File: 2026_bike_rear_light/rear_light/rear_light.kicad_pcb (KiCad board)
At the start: 2 copper layers, 22 parts, among them J1 Conn_01x04, J2 Conn_01x05, Q1 2N5551, Q2 FQP27P06, Q3 2N5551, Q4 FQP27P06, Q5 2N5551, Q6 2N5551, Q7 FQP27P06, U1 YAAJ_DCDC_StepDown_LM2596

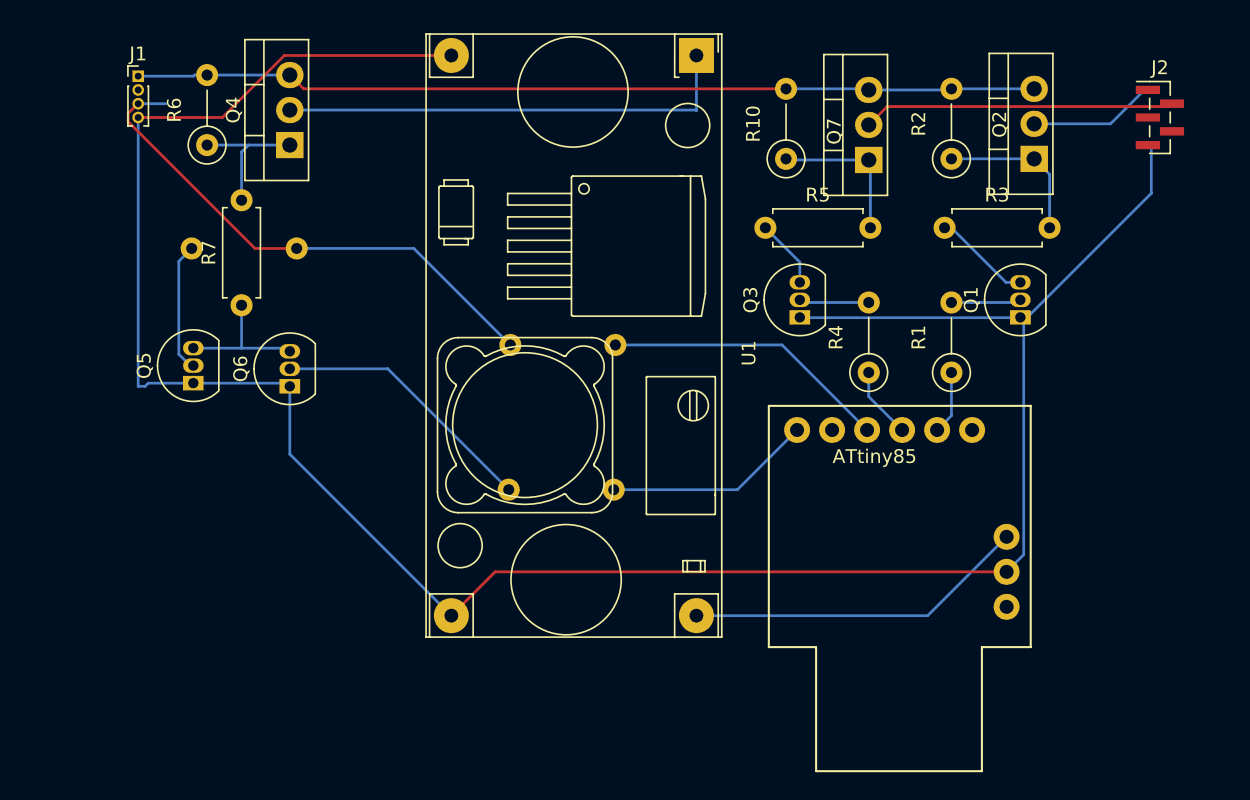
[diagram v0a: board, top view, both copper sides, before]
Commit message: Bike Rear Light - Update PCB for molex connectors
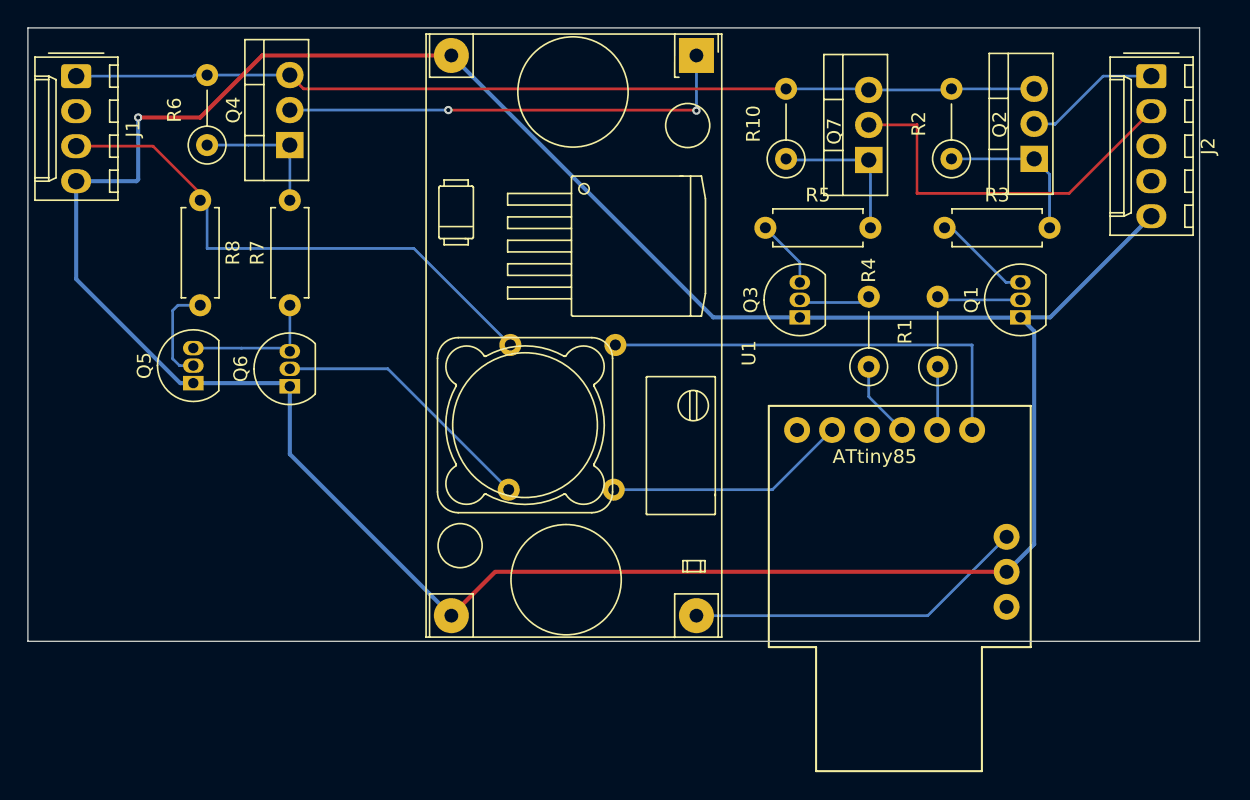
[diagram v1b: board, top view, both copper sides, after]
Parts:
- J1: footprint Connector_PinHeader_1.00mm:PinHeader_1x04_P1.00mm_Vertical -> Connector_Molex:Molex_KK-254_AE-6410-04A_1x04_P2.54mm_Vertical
- J2: footprint Connector_PinHeader_1.00mm:PinHeader_1x05_P1.00mm_Vertical_SMD_Pin1Left -> Connector_Molex:Molex_KK-254_AE-6410-05A_1x05_P2.54mm_Vertical
- R8: moved to F.Cu
- moved R8 7.83 mm to (65.5, 57.5), turned to -90 degrees
- moved J1 4.50 mm to (56.5, 48.5), turned to -90 degrees
- moved R7 3.50 mm to (72.0, 65.1)
- moved J2 3.06 mm to (134.5, 48.5), turned to -90 degrees
- moved R1 1.08 mm to (119.0, 69.6)
- moved R4 0.42 mm to (114.0, 69.6)
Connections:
- R11 pad 1: /PB3 -> /PB0
- R9 pad 1: /PB5 -> /PB4
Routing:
- net GND: track 170.4 -> 204.2 mm, vias 0 -> 1
- net /PB0: track 0.00 -> 32.0 mm
- net /PB3: track 20.8 -> 0.00 mm
- net /PB4: track 0.00 -> 17.6 mm
- net /PB5: track 15.1 -> 0.00 mm
- net /BRAKE: track 22.6 -> 28.0 mm
- net +48V: track 65.5 -> 70.0 mm
- net Net-(Q5-B): track 9.45 -> 7.86 mm
- net +5V: track 38.1 -> 39.5 mm
- net Net-(Q1-B): track 5.08 -> 6.35 mm
- net /TAIL: track 9.02 -> 9.97 mm
- net Net-(Q4-D): track 33.5 -> 33.6 mm, vias 0 -> 2
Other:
- board outline added: 85 x 44.5 mm

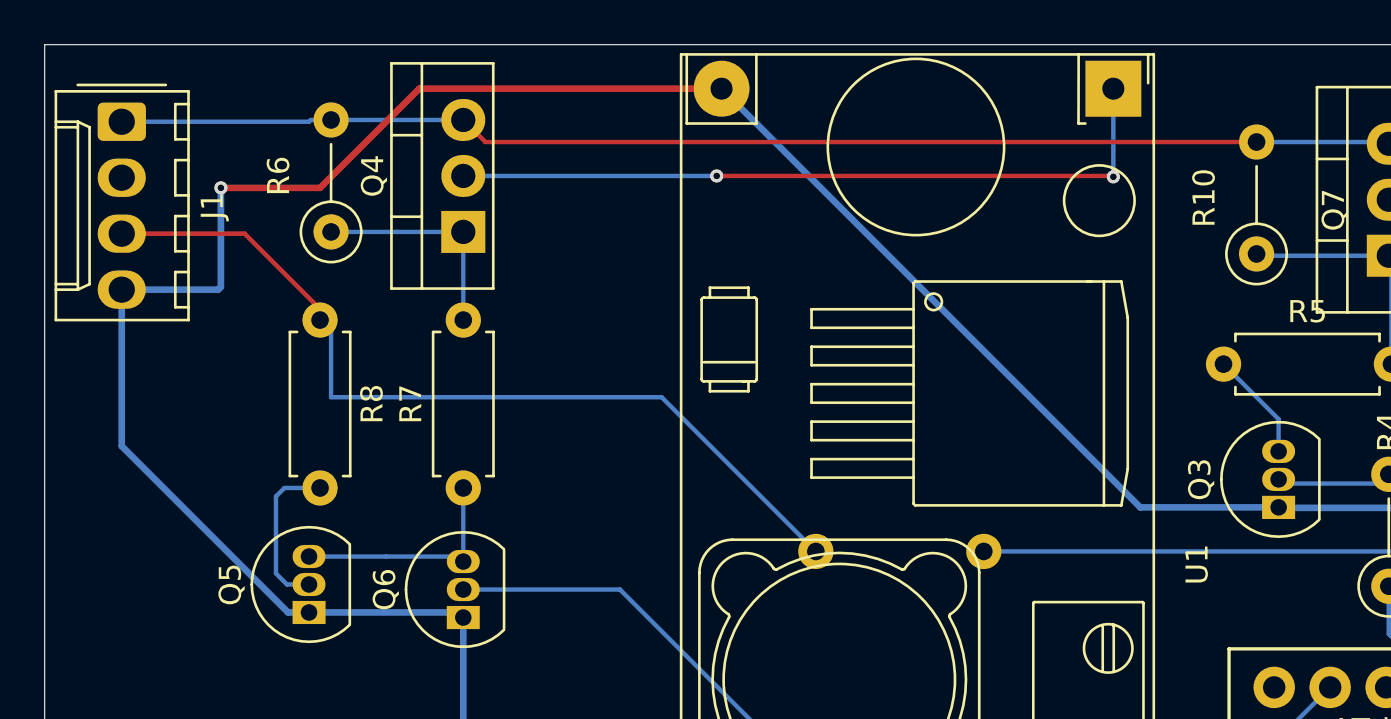
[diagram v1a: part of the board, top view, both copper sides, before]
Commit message: Bike Rear Light - Update Schematic and PCB (remove MOSFET)
 - Alter circuit so that it controls the buck converter via its enablement pin
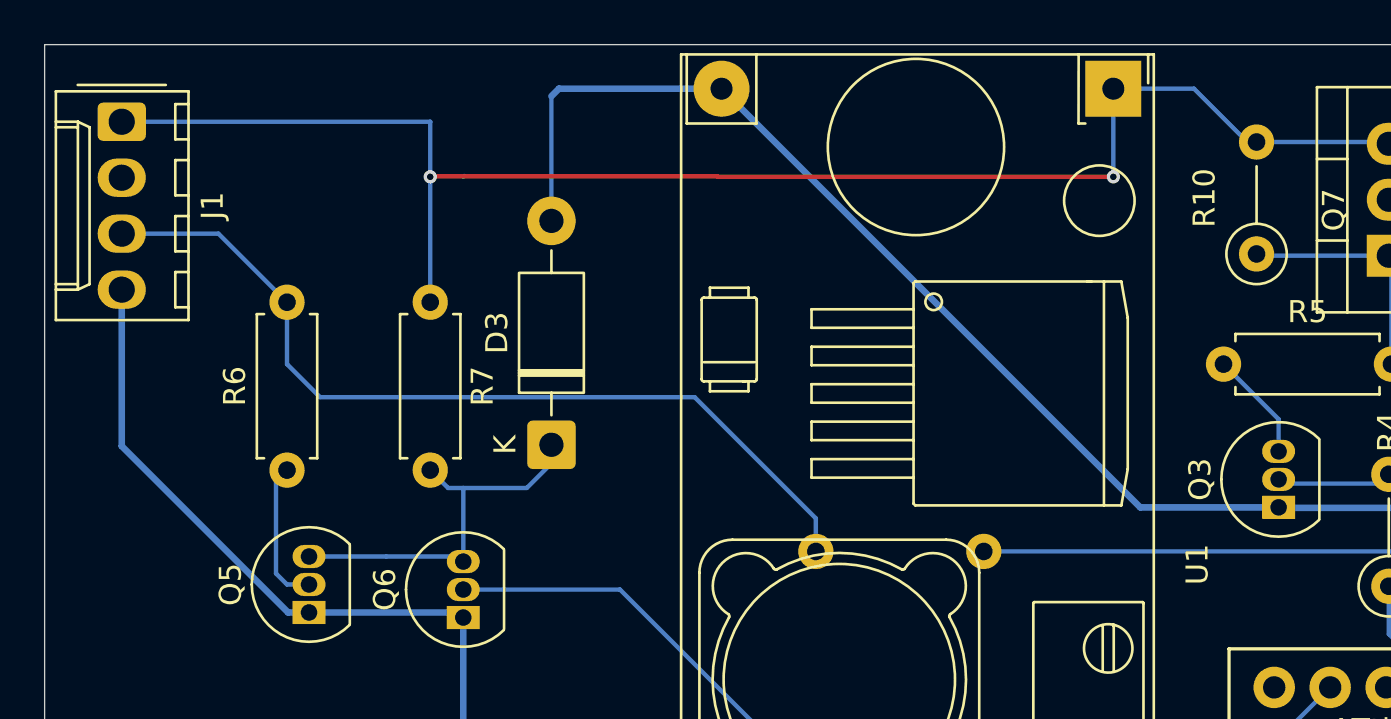
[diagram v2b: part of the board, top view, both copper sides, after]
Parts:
- removed Q4: FQP27P06, Package_TO_SOT_THT:TO-220-3_Vertical
- removed R8: 10k, Resistor_THT:R_Axial_DIN0207_L6.3mm_D2.5mm_P7.62mm_Horizontal
- added D3: D_Zener 12v, Diode_THT:D_DO-41_SOD81_P10.16mm_Horizontal, F.Cu at (76.0, 63.2)
- R6: value 4k7 -> 10k; footprint Resistor_THT:R_Axial_DIN0207_L6.3mm_D2.5mm_P5.08mm_Vertical -> Resistor_THT:R_Axial_DIN0207_L6.3mm_D2.5mm_P7.62mm_Horizontal
- R7: value 15k -> 100k
- moved R6 11.0 mm to (64.0, 64.3)
- moved R7 8.56 mm to (70.5, 56.7), turned to -90 degrees
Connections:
- Q5 pad 3: Net-(Q5-C) -> /U1_enable
- Q6 pad 3: Net-(Q5-C) -> /U1_enable
- R6 pad 1: Net-(Q4-G) -> Net-(Q5-B)
- R6 pad 2: +48V -> +5V
- R7 pad 1: Net-(Q5-C) -> +48V
- R7 pad 2: Net-(Q4-G) -> /U1_enable
- U1 pad 1: Net-(Q4-D) -> +48V
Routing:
- net Net-(Q4-D): track 33.6 -> 0.00 mm, vias 2 -> 0
- net GND: track 204.2 -> 184.1 mm, vias 1 -> 0
- net /U1_enable: track 0.00 -> 17.6 mm
- net +48V: track 70.0 -> 82.9 mm, vias 0 -> 2
- net Net-(Q5-C): track 10.4 -> 0.00 mm
- net Net-(Q4-G): track 10.0 -> 0.00 mm
- net Net-(Q5-B): track 7.86 -> 6.60 mm

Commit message: Bike Rear Light - Update circuit for new buck converter
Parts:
- removed U1: YAAJ_DCDC_StepDown_LM2596, models:YAAJ_DCDC_StepDown_LM2596
- added HT7886_module1: 5v, HT7886:DC-DC_100V_3.5A_step_down, F.Cu at (92.2, 71.0)
- added R8: 10k, Resistor_THT:R_Axial_DIN0207_L6.3mm_D2.5mm_P7.62mm_Horizontal, F.Cu at (77.0, 57.0)
- D3: value D_Zener 12v -> Zener 5v
- moved D3 18.7 mm to (70.5, 81.0)
- moved R7 17.6 mm to (65.0, 73.4)
- moved Q5 11.7 mm to (59.5, 81.0)
- moved Q6 11.0 mm to (76.5, 81.0)
- moved R6 8.16 mm to (59.5, 71.1)
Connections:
- D3 pad 1: /U1_enable -> Net-(D3-K)
- Q5 pad 1: GND -> Net-(D3-K)
- Q5 pad 3: /U1_enable -> Net-(Q5-C)
- Q6 pad 1: GND -> Net-(D3-K)
- Q6 pad 3: /U1_enable -> Net-(Q5-C)
- R7 pad 1: +48V -> GND
- R7 pad 2: /U1_enable -> Net-(D3-K)
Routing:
- net Net-(D3-K): track 0.00 -> 43.9 mm
- net VCC: track 0.00 -> 38.6 mm
- net GND: track 184.1 -> 151.8 mm
- net Net-(Q5-C): track 0.00 -> 31.1 mm
- net VIN: track 24.9 -> 0.00 mm
- net /U1_enable: track 17.6 -> 0.00 mm
- net Net-(Q6-B): track 19.5 -> 11.9 mm
- net +5V: track 40.0 -> 46.2 mm
- net Net-(Q5-B): track 6.60 -> 11.0 mm
- net +48V: track 82.9 -> 83.2 mm, vias 2 -> 0
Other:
- board text added: "2N5551"
